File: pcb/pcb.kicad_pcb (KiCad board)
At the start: 2 copper layers, 100 x 84 mm, 49 parts, among them SW1 MX_SWITCH, SW10 MX_SWITCH, SW11 MX_SWITCH, SW12 MX_SWITCH, SW13 MX_SWITCH, SW14 MX_SWITCH, SW15 MX_SWITCH, SW16 MX_SWITCH, SW2 MX_SWITCH, SW3 MX_SWITCH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

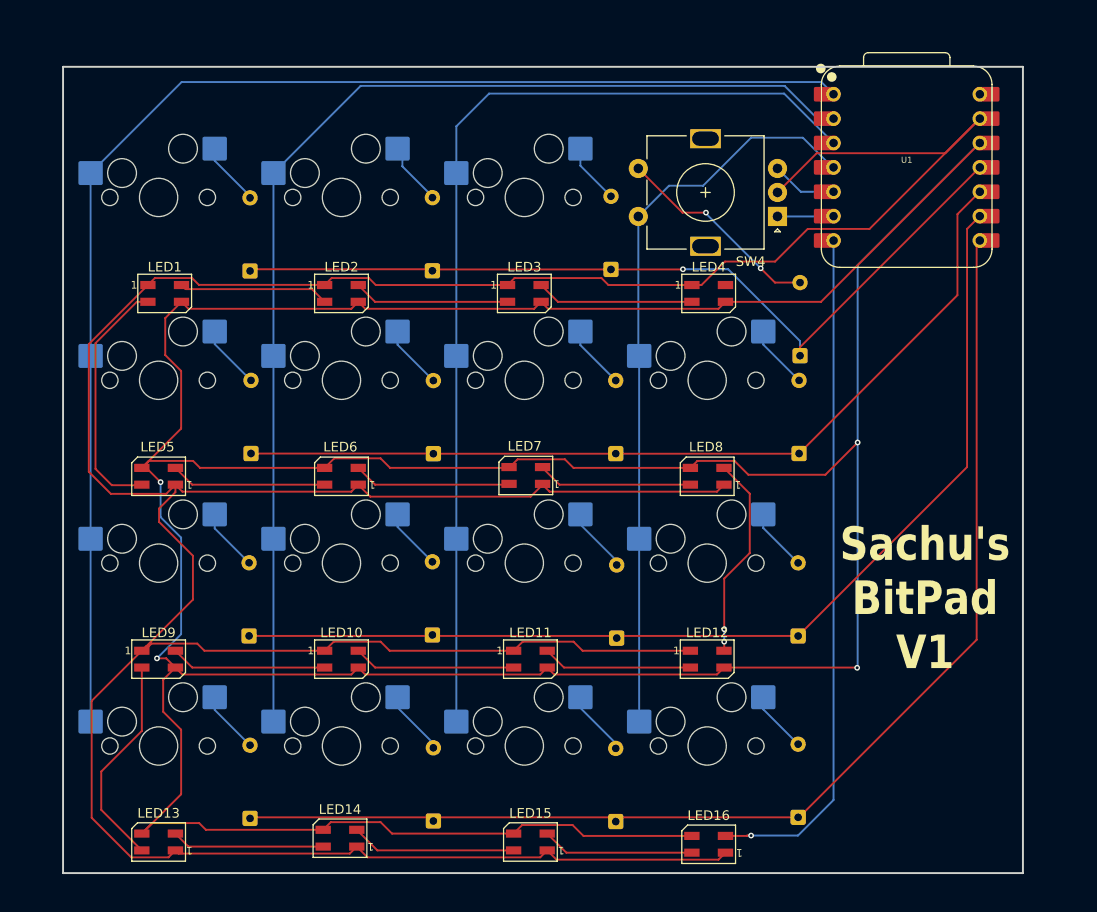
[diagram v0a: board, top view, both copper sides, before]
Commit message: update schematics and footprints to match sk6812mini-e
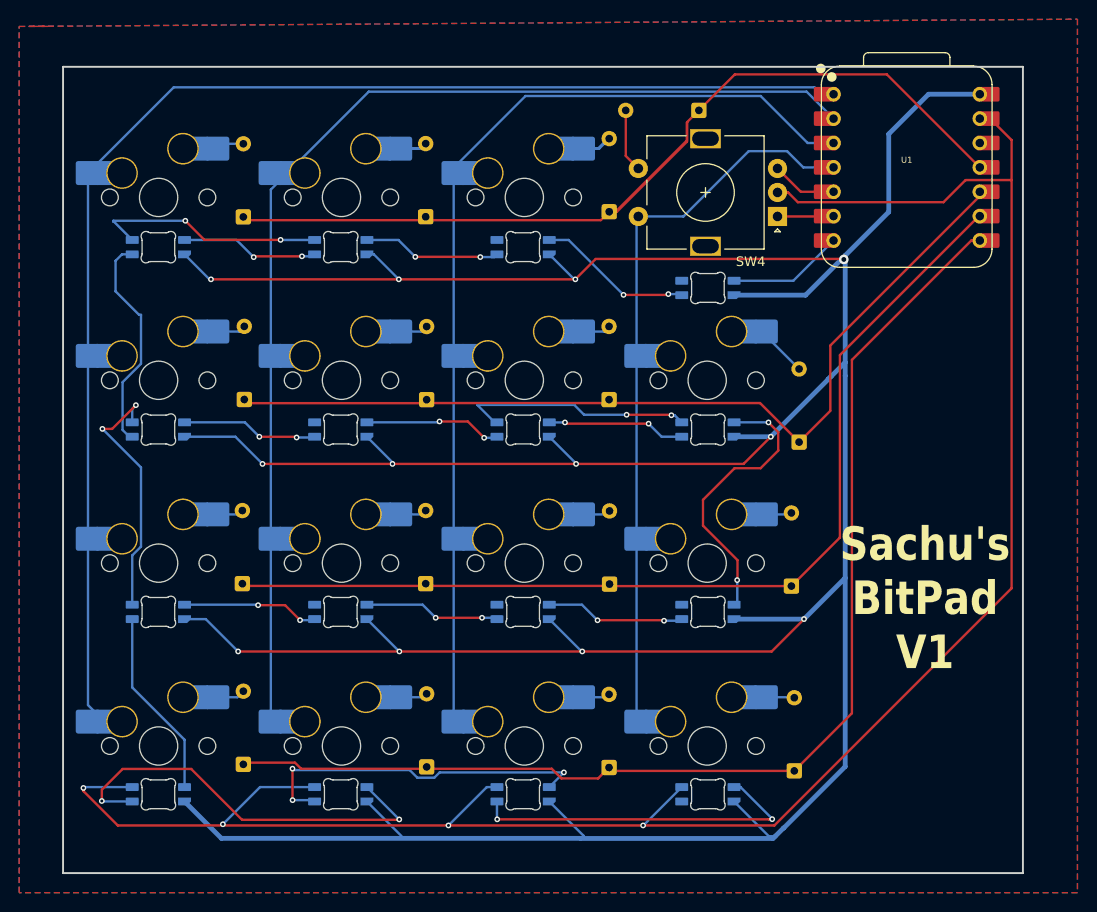
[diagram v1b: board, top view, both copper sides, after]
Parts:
- LED1, LED10, LED11, LED12, LED13, LED14, LED15, LED16, LED2, LED3, LED4, LED5, LED6, LED7, LED8, LED9: value SK6812MINI -> MX_SK6812MINI-E; footprint LED_SMD:LED_SK6812MINI_PLCC4_3.5x3.5mm_P1.75mm -> PCM_marbastlib-mx:LED_MX_6028R; moved to B.Cu
- SW1, SW10, SW11, SW12, SW13, SW14, SW15, SW16, SW2, SW3, SW5, SW6, SW7, SW8, SW9: footprint MX_Hotswap:MX-Hotswap-1U -> PCM_marbastlib-mx:SW_MX_HS_CPG151101S11_1u
- moved D4 27.6 mm to (161.1, 64.8), turned to 180 degrees
- moved D3 6.01 mm to (151.7, 75.3)
- moved D11 5.68 mm to (151.8, 114.1)
- moved D7 5.67 mm to (151.7, 94.9)
- moved D1 5.67 mm to (113.6, 75.8)
- moved D14 5.67 mm to (132.7, 133.2)
- moved D15 5.67 mm to (151.7, 133.2)
- moved D2 5.67 mm to (132.6, 75.8)
- moved D6 5.67 mm to (132.7, 94.9)
- moved D13 5.67 mm to (113.6, 132.9)
- moved D5 5.67 mm to (113.7, 94.9)
- moved D9 5.48 mm to (113.5, 114.1)
- moved D10 5.39 mm to (132.6, 114.1)
- moved D12 5.25 mm to (170.7, 114.3)
- moved LED16 5.21 mm to (162.0, 136.0)
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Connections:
- LED1 pad 2: Net-(LED1-DIN) -> Net-(LED1-DOUT)
- LED1 pad 3: +3.3V -> Net-(LED1-DIN)
- LED1 pad 4: Net-(LED1-DOUT) -> +5V
- LED10 pad 2: Net-(LED10-DIN) -> Net-(LED10-DOUT)
- LED10 pad 3: +3.3V -> Net-(LED10-DIN)
- LED10 pad 4: Net-(LED10-DOUT) -> +5V
- LED11 pad 2: Net-(LED10-DOUT) -> Net-(LED10-DIN)
- LED11 pad 3: +3.3V -> Net-(LED11-DIN)
- LED11 pad 4: Net-(LED11-DOUT) -> +5V
- LED12 pad 2: Net-(LED11-DOUT) -> Net-(LED11-DIN)
- LED12 pad 3: +3.3V -> Net-(LED12-DIN)
- LED12 pad 4: Net-(LED12-DOUT) -> +5V
- LED13 pad 2: Net-(LED13-DIN) -> Net-(LED13-DOUT)
- LED13 pad 3: +3.3V -> Net-(LED13-DIN)
- LED13 pad 4: Net-(LED13-DOUT) -> +5V
- LED14 pad 2: Net-(LED14-DIN) -> Net-(LED14-DOUT)
- LED14 pad 3: +3.3V -> Net-(LED13-DOUT)
- LED14 pad 4: Net-(LED13-DIN) -> +5V
- LED15 pad 2: Net-(LED15-DIN) -> Net-(LED15-DOUT)
- LED15 pad 3: +3.3V -> Net-(LED14-DOUT)
- LED15 pad 4: Net-(LED14-DIN) -> +5V
- LED16 pad 2: led -> unconnected-(LED16-DOUT-Pad2)
- LED16 pad 3: +3.3V -> Net-(LED15-DOUT)
- LED16 pad 4: Net-(LED15-DIN) -> +5V
- LED2 pad 2: Net-(LED1-DOUT) -> Net-(LED1-DIN)
- LED2 pad 3: +3.3V -> Net-(LED2-DIN)
- LED2 pad 4: Net-(LED2-DOUT) -> +5V
- LED3 pad 2: Net-(LED2-DOUT) -> Net-(LED2-DIN)
- LED3 pad 3: +3.3V -> Net-(LED3-DIN)
- LED3 pad 4: Net-(LED3-DOUT) -> +5V
- LED4 pad 2: Net-(LED3-DOUT) -> Net-(LED3-DIN)
- LED4 pad 3: +3.3V -> led
- LED4 pad 4: unconnected-(LED4-DOUT-Pad4) -> +5V
- LED5 pad 2: Net-(LED5-DIN) -> Net-(LED1-DOUT)
- LED5 pad 3: +3.3V -> Net-(LED5-DIN)
- LED5 pad 4: Net-(LED1-DIN) -> +5V
- LED6 pad 2: Net-(LED6-DIN) -> Net-(LED5-DIN)
- LED6 pad 3: +3.3V -> Net-(LED6-DIN)
- LED6 pad 4: Net-(LED5-DIN) -> +5V
- LED7 pad 2: Net-(LED7-DIN) -> Net-(LED6-DIN)
- LED7 pad 3: +3.3V -> Net-(LED7-DIN)
- LED7 pad 4: Net-(LED6-DIN) -> +5V
- LED8 pad 2: Net-(LED12-DOUT) -> Net-(LED7-DIN)
- LED8 pad 3: +3.3V -> Net-(LED12-DIN)
- LED8 pad 4: Net-(LED7-DIN) -> +5V
- LED9 pad 2: Net-(LED13-DOUT) -> Net-(LED13-DIN)
- LED9 pad 3: +3.3V -> Net-(LED10-DOUT)
- LED9 pad 4: Net-(LED10-DIN) -> +5V
- U1 pad 12: +3.3V -> unconnected-(U1-3V3-Pad12)_1
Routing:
- net +5V: track 0.00 -> 437.8 mm, vias 0 -> 12
- net +3.3V: track 429.2 -> 0.00 mm, vias 4 -> 0
- net GND: track 382.2 -> 290.5 mm, vias 0 -> 10
- net led: track 71.3 -> 12.1 mm, vias 1 -> 0
- net Net-(LED14-DOUT): track 0.00 -> 36.7 mm, vias 0 -> 3
- net Net-(LED15-DOUT): track 0.00 -> 35.9 mm, vias 0 -> 2
- net Net-(LED12-DIN): track 0.00 -> 29.5 mm, vias 0 -> 2
- net Net-(LED12-DOUT): track 21.3 -> 0.00 mm, vias 2 -> 0
- net Net-(LED13-DOUT): track 22.6 -> 43.2 mm, vias 0 -> 2
- net Net-(LED14-DIN): track 17.2 -> 0.00 mm
- net Net-(LED3-DOUT): track 16.4 -> 0.00 mm
- net Net-(LED2-DOUT): track 16.3 -> 0.00 mm
- net Net-(LED3-DIN): track 0.00 -> 16.2 mm, vias 0 -> 2
- net Net-(LED15-DIN): track 15.9 -> 0.00 mm
- net Net-(LED11-DOUT): track 15.6 -> 0.00 mm
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- added copper zone on B.Cu, net GND
- added copper zone on F.Cu, net GND
